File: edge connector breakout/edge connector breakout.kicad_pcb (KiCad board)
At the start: 2 copper layers, 50.8 x 58.4 mm, 2 parts, among them J1 C64 Card Edge, J2 0.1" header

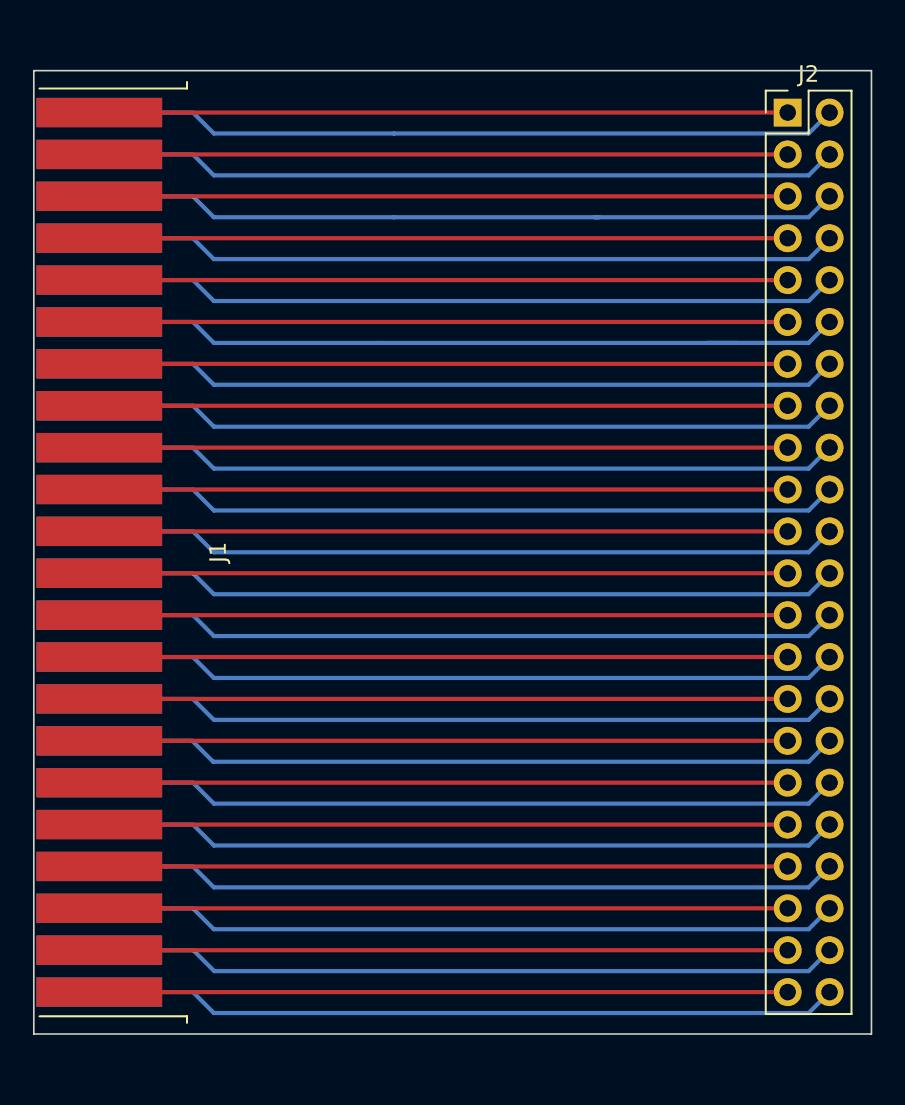
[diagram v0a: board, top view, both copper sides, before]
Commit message: breakout pcb: add silkscreen labels for all pins
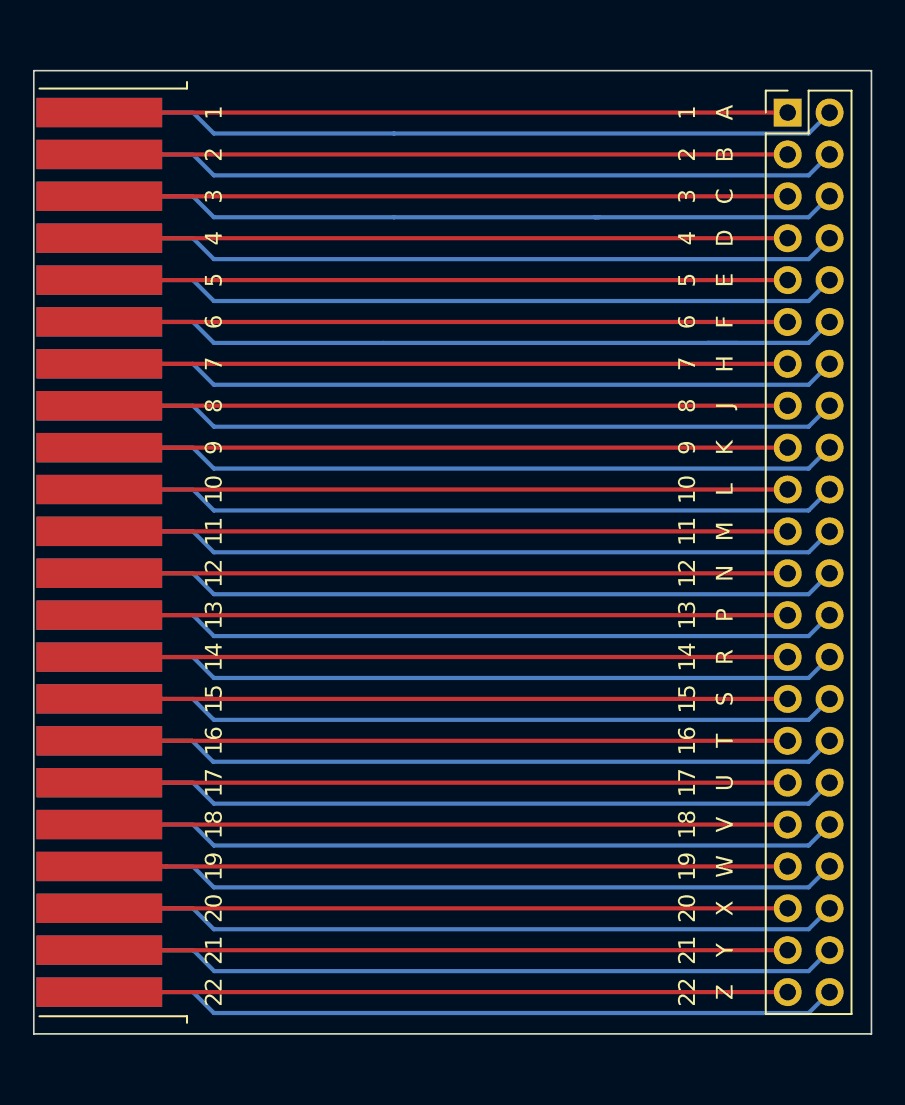
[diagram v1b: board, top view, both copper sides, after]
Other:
- board text added: "1"
- board text added: "10"
- board text added: "11"
- board text added: "12"
- board text added: "13"
- board text added: "14"
- board text added: "15"
- board text added: "16"
- board text added: "17"
- board text added: "18"
- board text added: "19"
- board text added: "2"
- board text added: "20"
- board text added: "21"
- board text added: "22"
- board text added: "3"
- board text added: "4"
- board text added: "5"
- board text added: "6"
- board text added: "7"
- board text added: "8"
- board text added: "9"
- board text added: "A"
- board text added: "B"
- board text added: "C"
- board text added: "D"
- board text added: "E"
- board text added: "F"
- board text added: "H"
- board text added: "J"
- board text added: "K"
- board text added: "L"
- board text added: "M"
- board text added: "N"
- board text added: "P"
- board text added: "R"
- board text added: "S"
- board text added: "T"
- board text added: "U"
- board text added: "V"
- board text added: "W"
- board text added: "X"
- board text added: "Y"
- board text added: "Z"

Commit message: Import CBM logo; place logo, serial, copyright
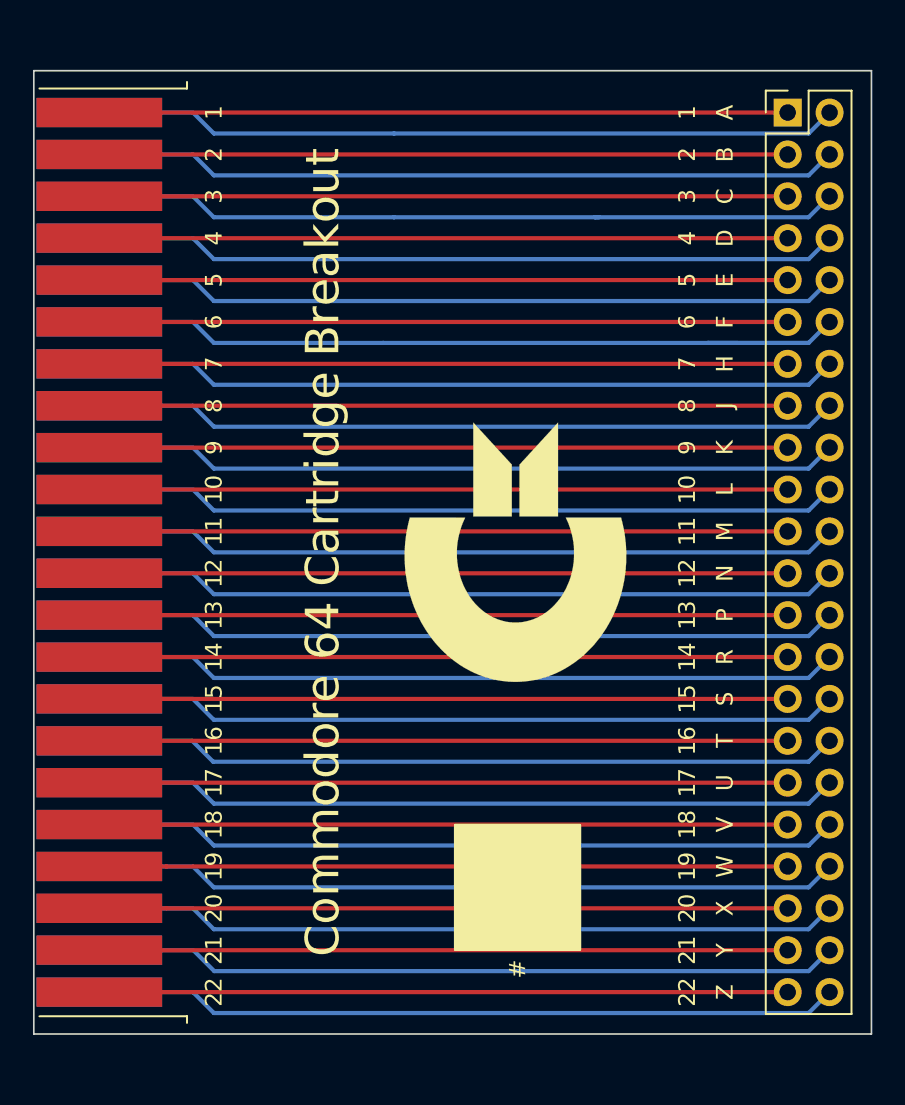
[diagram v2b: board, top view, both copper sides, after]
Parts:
- added G***: LOGO, Commodore:CBM_Logo_16mm, F.Cu at (54.6, 52.1)
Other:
- board text added: "#"
- board text added: "Commodore 64 Cartridge Breakout"
- board text added: "© 2020 Matt Mullins No Rights Reserved"
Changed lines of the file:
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@@
   (general
     (thickness 1.6)
-    (drawings 92)
+    (drawings 96)
     (tracks 130)
     (zones 0)
-    (modules 2)
+    (modules 3)
     (nets 45)
   )
@@
     (add_net /Y)
     (add_net /Z)
+  )
+  (module Commodore:CBM_Logo_16mm (layer F.Cu)
+    (at 54.61 52.07 90)
+    (fp_text reference G*** (at 0 0 90) (layer F.SilkS) hide
+      (effects (font (size 1.524 1.524) (thickness 0.3)))
+    )
+    (fp_text value LOGO (at 0.75 0 90) (layer F.SilkS) hide
+      (effects (font (size 1.524 1.524) (thickness 0.3)))
+    )
+    (fp_poly (pts (xy 0.153666 -6.714869) (xy 0.524464 -6.691241) (xy 0.89294 -6.651833) (xy 1.258078 -6.596638)
+      (xy 1.61886 -6.525651) (xy 1.8669 -6.466909) (xy 1.920522 -6.453321) (xy 1.970824 -6.440608)
+      (xy 2.014652 -6.429563) (xy 2.048854 -6.42098) (xy 2.070277 -6.415655) (xy 2.072217 -6.41518)
+      (xy 2.1082 -6.406414) (xy 2.1082 -4.726301) (xy 2.108181 -4.521242) (xy 2.108123 -4.332524)
+      (xy 2.108021 -4.159555) (xy 2.107872 -4.001744) (xy 2.107671 -3.858498) (xy 2.107416 -3.729225)
+      (xy 2.107102 -3.613334) (xy 2.106726 -3.510232) (xy 2.106284 -3.419327) (xy 2.105772 -3.340028)
+      (xy 2.105187 -3.271742) (xy 2.104525 -3.213878) (xy 2.103781 -3.165843) (xy 2.102953 -3.127045)
+      (xy 2.102036 -3.096893) (xy 2.101028 -3.074794) (xy 2.099923 -3.060157) (xy 2.098719 -3.052389)
+      (xy 2.097617 -3.050745) (xy 2.086786 -3.055667) (xy 2.063314 -3.066492) (xy 2.029908 -3.081967)
+      (xy 1.989274 -3.100837) (xy 1.951567 -3.118381) (xy 1.70968 -3.222604) (xy 1.462164 -3.312488)
+      (xy 1.208018 -3.388292) (xy 0.94624 -3.450276) (xy 0.675831 -3.498699) (xy 0.395788 -3.533823)
+      (xy 0.325967 -3.540396) (xy 0.275742 -3.543788) (xy 0.211898 -3.546486) (xy 0.137568 -3.548491)
+      (xy 0.055883 -3.549802) (xy -0.030022 -3.550418) (xy -0.117015 -3.550341) (xy -0.201963 -3.549568)
+      (xy -0.281734 -3.5481) (xy -0.353194 -3.545937) (xy -0.41321 -3.543078) (xy -0.448733 -3.540485)
+      (xy -0.739064 -3.506954) (xy -1.02018 -3.459327) (xy -1.292418 -3.397492) (xy -1.556117 -3.321334)
+      (xy -1.811614 -3.230738) (xy -2.059249 -3.12559) (xy -2.29936 -3.005776) (xy -2.532284 -2.871182)
+      (xy -2.645833 -2.798521) (xy -2.776369 -2.70924) (xy -2.895625 -2.620993) (xy -3.008508 -2.529838)
+      (xy -3.119923 -2.431835) (xy -3.220648 -2.3368) (xy -3.390966 -2.160744) (xy -3.54691 -1.977185)
+      (xy -3.688186 -1.786626) (xy -3.814498 -1.589567) (xy -3.92555 -1.386509) (xy -4.021047 -1.177954)
+      (xy -4.100693 -0.964403) (xy -4.164194 -0.746358) (xy -4.168746 -0.72801) (xy -4.195454 -0.61221)
+      (xy -4.21641 -0.504964) (xy -4.232145 -0.401718) (xy -4.243193 -0.297919) (xy -4.250084 -0.189014)
+      (xy -4.25335 -0.070448) (xy -4.253794 0) (xy -4.253097 0.101473) (xy -4.250713 0.190248)
+      (xy -4.246255 0.270512) (xy -4.239335 0.34645) (xy -4.229568 0.422247) (xy -4.216565 0.50209)
+      (xy -4.199941 0.590165) (xy -4.19865 0.596654) (xy -4.145491 0.820134) (xy -4.076292 1.038671)
+      (xy -3.991332 1.251838) (xy -3.890892 1.459209) (xy -3.77525 1.660356) (xy -3.644686 1.854854)
+      (xy -3.499479 2.042276) (xy -3.33991 2.222196) (xy -3.166258 2.394185) (xy -2.978803 2.55782)
+      (xy -2.843498 2.66417) (xy -2.703638 2.765108) (xy -2.561706 2.858341) (xy -2.413458 2.946458)
+      (xy -2.254651 3.032045) (xy -2.1717 3.073841) (xy -1.948666 3.177104) (xy -1.724196 3.267122)
+      (xy -1.496178 3.344493) (xy -1.262502 3.409813) (xy -1.021055 3.46368) (xy -0.769728 3.506691)
+      (xy -0.537633 3.536152) (xy -0.485213 3.540593) (xy -0.418752 3.544319) (xy -0.341132 3.547315)
+      (xy -0.25523 3.549568) (xy -0.163927 3.551062) (xy -0.070101 3.551782) (xy 0.023369 3.551716)
+      (xy 0.113603 3.550846) (xy 0.197721 3.54916) (xy 0.272846 3.546643) (xy 0.336097 3.543279)
+      (xy 0.3683 3.540742) (xy 0.654759 3.506371) (xy 0.933341 3.457196) (xy 1.204699 3.39304)
+      (xy 1.469486 3.31373) (xy 1.728355 3.219087) (xy 1.981959 3.108937) (xy 1.996017 3.102308)
+      (xy 2.1082 3.049178) (xy 2.1082 6.406664) (xy 1.864784 6.466706) (xy 1.64196 6.519316)
+      (xy 1.429427 6.564441) (xy 1.222681 6.602833) (xy 1.017217 6.635242) (xy 0.808531 6.662421)
+      (xy 0.592119 6.685119) (xy 0.512233 6.692271) (xy 0.34621 6.704362) (xy 0.168536 6.71337)
+      (xy -0.015774 6.719205) (xy -0.201703 6.721776) (xy -0.384235 6.720993) (xy -0.558354 6.716764)
+      (xy -0.643467 6.713194) (xy -1.014595 6.687038) (xy -1.383585 6.64495) (xy -1.749575 6.587153)
+      (xy -2.111704 6.513873) (xy -2.469113 6.425333) (xy -2.820941 6.321758) (xy -3.166327 6.203372)
+      (xy -3.504411 6.0704) (xy -3.834333 5.923067) (xy -4.017433 5.83324) (xy -4.329002 5.666828)
+      (xy -4.628503 5.489493) (xy -4.917748 5.300014) (xy -5.198547 5.097172) (xy -5.472709 4.879747)
+      (xy -5.6261 4.749351) (xy -5.667676 4.712063) (xy -5.718468 4.66477) (xy -5.776378 4.609565)
+      (xy -5.839309 4.54854) (xy -5.905164 4.483788) (xy -5.971844 4.4174) (xy -6.037252 4.351469)
+      (xy -6.09929 4.288087) (xy -6.15586 4.229347) (xy -6.204866 4.177341) (xy -6.244209 4.134161)
+      (xy -6.253792 4.123267) (xy -6.47365 3.858783) (xy -6.677378 3.589253) (xy -6.864967 3.314695)
+      (xy -7.036406 3.035128) (xy -7.191688 2.75057) (xy -7.330802 2.461038) (xy -7.453739 2.166553)
+      (xy -7.56049 1.86713) (xy -7.651046 1.56279) (xy -7.725397 1.25355) (xy -7.734335 1.210733)
+      (xy -7.790185 0.896768) (xy -7.829239 0.582509) (xy -7.851613 0.268421) (xy -7.857428 -0.045028)
+      (xy -7.846804 -0.357371) (xy -7.819857 -0.668142) (xy -7.776707 -0.976872) (xy -7.717474 -1.283096)
+      (xy -7.642275 -1.586347) (xy -7.55123 -1.886157) (xy -7.444459 -2.182059) (xy -7.322079 -2.473587)
+      (xy -7.184209 -2.760273) (xy -7.03097 -3.041651) (xy -6.862478 -3.317253) (xy -6.678854 -3.586613)
+      (xy -6.480216 -3.849264) (xy -6.430037 -3.9116) (xy -6.262733 -4.108448) (xy -6.082141 -4.305096)
+      (xy -5.891612 -4.498203) (xy -5.694497 -4.684426) (xy -5.494148 -4.860424) (xy -5.401733 -4.937103)
+      (xy -5.123307 -5.152921) (xy -4.833688 -5.356312) (xy -4.533533 -5.546946) (xy -4.223503 -5.72449)
+      (xy -3.904254 -5.888613) (xy -3.576446 -6.038983) (xy -3.240739 -6.175267) (xy -2.897789 -6.297133)
+      (xy -2.548256 -6.404251) (xy -2.421466 -6.438999) (xy -2.062901 -6.525641) (xy -1.699537 -6.596551)
+      (xy -1.332391 -6.651721) (xy -0.962481 -6.691144) (xy -0.590823 -6.714814) (xy -0.218435 -6.722724)
+      (xy 0.153666 -6.714869)) (layer F.SilkS) (width 0.01))
+    (fp_poly (pts (xy 7.866244 2.582333) (xy 2.175934 2.582333) (xy 2.175934 0.245533) (xy 5.317092 0.245533)
+      (xy 7.866244 2.582333)) (layer F.SilkS) (width 0.01))
+    (fp_poly (pts (xy 5.02285 -2.556895) (xy 7.869767 -2.556857) (xy 7.818967 -2.511193) (xy 7.807658 -2.500913)
+      (xy 7.784502 -2.479762) (xy 7.750129 -2.448317) (xy 7.705169 -2.407156) (xy 7.650252 -2.356856)
+      (xy 7.586007 -2.297994) (xy 7.513064 -2.231148) (xy 7.432054 -2.156896) (xy 7.343606 -2.075813)
+      (xy 7.24835 -1.988479) (xy 7.146915 -1.89547) (xy 7.039932 -1.797364) (xy 6.928031 -1.694738)
+      (xy 6.811841 -1.58817) (xy 6.691993 -1.478236) (xy 6.569115 -1.365514) (xy 6.544733 -1.343146)
+      (xy 5.3213 -0.220764) (xy 3.748617 -0.220449) (xy 2.175934 -0.220133) (xy 2.175934 -2.556934)
+      (xy 5.02285 -2.556895)) (layer F.SilkS) (width 0.01))
   )
   (module Commodore:Expansion_Cartridge (layer F.Cu)
@@
     )
   )
+  (gr_text "© 2020 Matt Mullins\nNo Rights Reserved" (at 64.008 52.07 90) (layer B.SilkS)
+    (effects (font (size 1 1) (thickness 0.15)) (justify mirror))
+  )
+  (gr_text "#" (at 54.737 77.343 90) (layer F.SilkS)
+    (effects (font (size 1 1) (thickness 0.15)))
+  )
+  (gr_poly (pts (xy 58.547 76.2) (xy 50.927 76.2) (xy 50.927 68.58) (xy 58.547 68.58)) (layer F.SilkS) (width 0.1))
+  (gr_text "Commodore 64 Cartridge Breakout" (at 42.926 52.07 90) (layer F.SilkS)
+    (effects (font (size 2.032 2.032) (thickness 0.3)))
+  )
   (gr_text K (at 36.322 45.72 90) (layer B.SilkS)

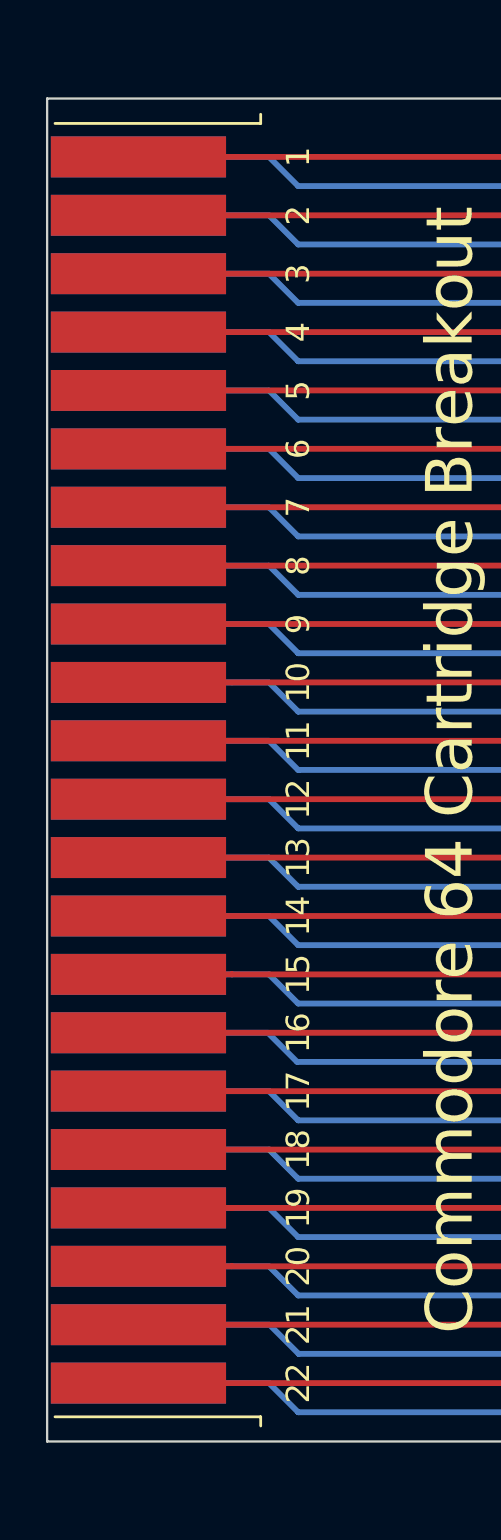
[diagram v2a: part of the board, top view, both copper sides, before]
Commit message: Mirror the edge connector in library, reset origin
Origin of the footprint is now the center of pin 1.  I don't know how
this ever looked right on the PCB layout itself, the footprint hasn't
been changed since "Initial commit".  But somewhere along the line I
definitely got the board-edge and the circuit side exactly backwards...
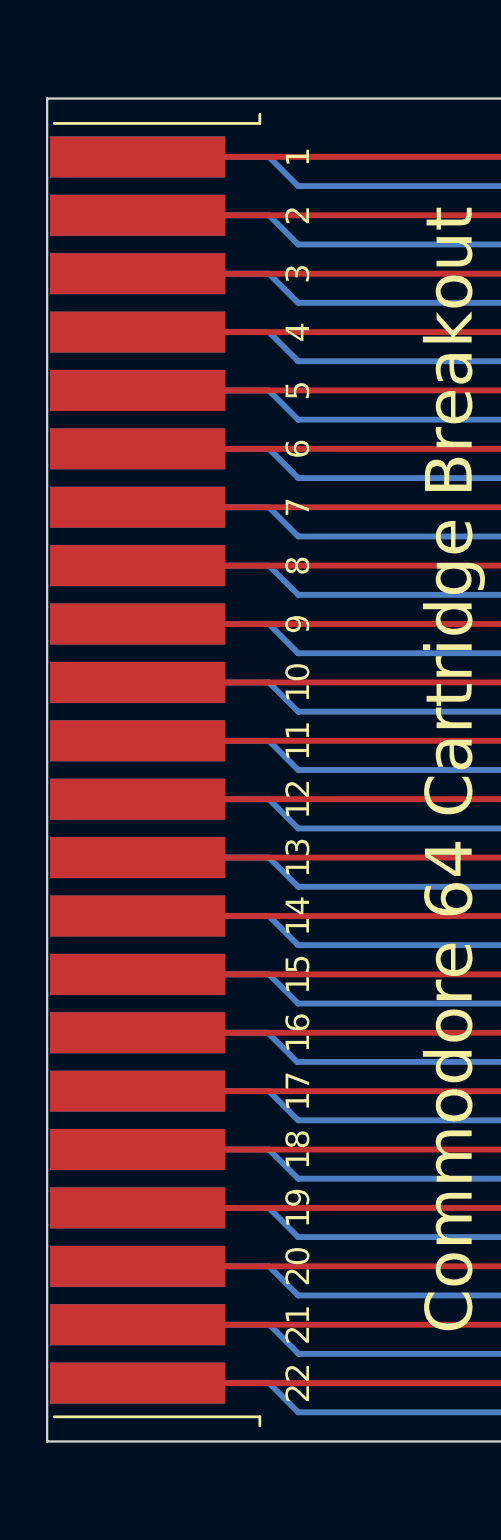
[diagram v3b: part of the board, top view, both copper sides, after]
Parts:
- moved J1 4.24 mm to (29.4, 25.4)
